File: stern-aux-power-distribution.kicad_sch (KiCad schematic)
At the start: 10 parts, among them J1 Conn_01x04, J2 Conn_01x02_Pin, J3 Conn_01x02_Pin, J4 Conn_01x02_Pin, J5 Conn_01x02_Pin

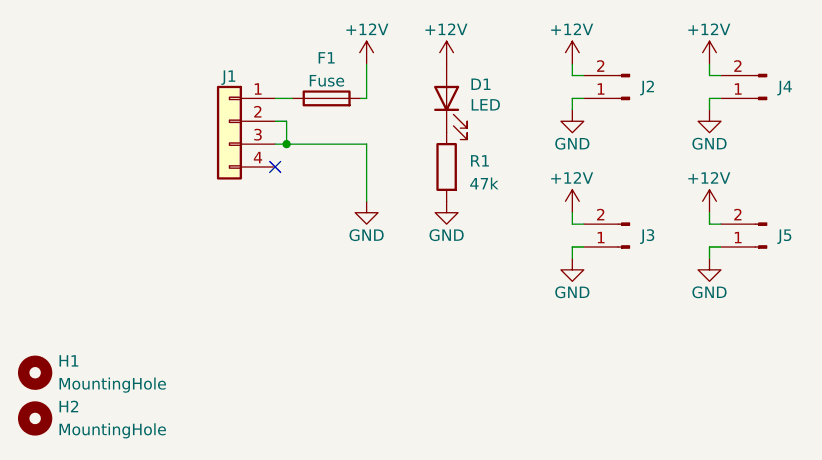
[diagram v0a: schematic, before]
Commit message: More silkscreen info
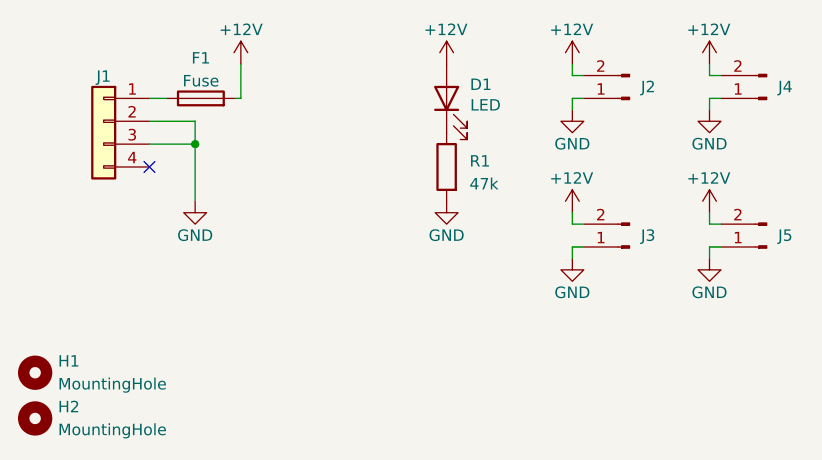
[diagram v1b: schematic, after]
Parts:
- H1, H2: footprint MountingHole:MountingHole_4mm -> MountingHole:MountingHole_4.3mm_M4
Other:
- moved on the sheet: F1, J1
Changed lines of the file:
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@@
 	(paper "A4")
 	(junction
-		(at 92.71 43.18)
+		(at 82.55 43.18)
 		(diameter 0)
 		(color 0 0 0 0)
 	)
 	(no_connect
-		(at 91.44 45.72)
+		(at 77.47 45.72)
 	)
 	(wire
@@
 	(wire
 		(pts
-			(xy 92.71 43.18) (xy 101.6 43.18)
+			(xy 86.995 38.1) (xy 87.63 38.1)
 		)
 		(stroke
@@
 	(wire
 		(pts
-			(xy 101.6 49.53) (xy 101.6 43.18)
+			(xy 82.55 49.53) (xy 82.55 43.18)
 		)
 		(stroke
@@
 	(wire
 		(pts
-			(xy 101.6 34.29) (xy 101.6 38.1)
-		)
-		(stroke
-			(width 0)
-			(type default)
-		)
-	)
-	(wire
-		(pts
-			(xy 91.44 40.64) (xy 92.71 40.64)
+			(xy 87.63 34.29) (xy 87.63 38.1)
+		)
+		(stroke
+			(width 0)
+			(type default)
+		)
+	)
+	(wire
+		(pts
+			(xy 77.47 40.64) (xy 82.55 40.64)
 		)
 		(stroke
@@
 	(wire
 		(pts
-			(xy 101.6 38.1) (xy 100.965 38.1)
-		)
-		(stroke
-			(width 0)
-			(type default)
-		)
-	)
-	(wire
-		(pts
-			(xy 91.44 38.1) (xy 93.345 38.1)
-		)
-		(stroke
-			(width 0)
-			(type default)
-		)
-	)
-	(wire
-		(pts
-			(xy 92.71 43.18) (xy 91.44 43.18)
+			(xy 77.47 38.1) (xy 79.375 38.1)
+		)
+		(stroke
+			(width 0)
+			(type default)
+		)
+	)
+	(wire
+		(pts
+			(xy 77.47 43.18) (xy 82.55 43.18)
 		)
 		(stroke
@@
 	(wire
 		(pts
-			(xy 92.71 40.64) (xy 92.71 43.18)
+			(xy 82.55 40.64) (xy 82.55 43.18)
 		)
 		(stroke
@@
 			)
 		)
-		(property "Footprint" "MountingHole:MountingHole_4mm"
+		(property "Footprint" "MountingHole:MountingHole_4.3mm_M4"
 			(at 64.77 73.66 0)
 			(effects
@@
 	(symbol
 		(lib_id "Device:Fuse")
-		(at 97.155 38.1 90)
+		(at 83.185 38.1 90)
 		(unit 1)
 		(exclude_from_sim no)
@@
 		(fields_autoplaced yes)
 		(property "Reference" "F1"
-			(at 97.155 33.6382 90)
+			(at 83.185 33.6382 90)
 			(effects
 				(font
@@
 		)
 		(property "Value" "Fuse"
-			(at 97.155 36.1751 90)
+			(at 83.185 36.1751 90)
 			(effects
 				(font
@@
 		)
 		(property "Footprint" "Custom_parts:Fuse holder Keystone 3557-2"
-			(at 97.155 39.878 90)
+			(at 83.185 39.878 90)
 			(effects
 				(font
@@
 		)
 		(property "Datasheet" "~"
-			(at 97.155 38.1 0)
+			(at 83.185 38.1 0)
 			(effects
 				(font
@@
 		)
 		(property "Description" ""
-			(at 97.155 38.1 0)
+			(at 83.185 38.1 0)
 			(effects
 				(font
@@
 	(symbol
 		(lib_id "power:+12V")
-		(at 101.6 34.29 0)
+		(at 87.63 34.29 0)
 		(unit 1)
 		(exclude_from_sim no)
@@
 		(on_board yes)
 		(dnp no)
-		(property "Reference" "#PWR01"
-			(at 101.6 38.1 0)
+		(property "Reference" "#PWR02"
+			(at 87.63 38.1 0)
 			(effects
 				(font
@@
 		)
 		(property "Value" "+12V"
-			(at 101.6 30.48 0)
+			(at 87.63 30.48 0)
 			(effects
 				(font
@@
 		)
 		(property "Footprint" ""
-			(at 101.6 34.29 0)
+			(at 87.63 34.29 0)
 			(effects
 				(font
@@
 		)
 		(property "Datasheet" ""
-			(at 101.6 34.29 0)
+			(at 87.63 34.29 0)
 			(effects
 				(font
@@
 		)
 		(property "Description" ""
-			(at 101.6 34.29 0)
+			(at 87.63 34.29 0)
 			(effects
 				(font
@@
 			(project ""
 				(path "/4265d214-fcee-41c6-a88d-6c6bd3f38fd2"
-					(reference "#PWR01")
+					(reference "#PWR02")
 					(unit 1)
 				)
@@
 	(symbol
 		(lib_id "Connector_Generic:Conn_01x04")
-		(at 86.36 40.64 0)
+		(at 72.39 40.64 0)
 		(mirror y)
 		(unit 1)
@@
 		(fields_autoplaced yes)
 		(property "Reference" "J1"
-			(at 86.36 35.6672 0)
+			(at 72.39 35.6672 0)
 			(effects
 				(font
@@
 		)
 		(property "Value" "Conn_01x04"
-			(at 86.36 35.6671 0)
+			(at 72.39 35.6671 0)
 			(effects
 				(font
@@
 		)
 		(property "Footprint" "Connector_TE-Connectivity:TE_MATE-N-LOK_350211-1_1x04_P5.08mm_Vertical"
-			(at 86.36 40.64 0)
+			(at 72.39 40.64 0)
 			(effects
 				(font
@@
 		)
 		(property "Datasheet" "~"
-			(at 86.36 40.64 0)
+			(at 72.39 40.64 0)
 			(effects
 				(font
@@
 		)
 		(property "Description" ""
-			(at 86.36 40.64 0)
+			(at 72.39 40.64 0)
 			(effects
 				(font
@@
 			)
 		)
-		(property "Footprint" "MountingHole:MountingHole_4mm"
+		(property "Footprint" "MountingHole:MountingHole_4.3mm_M4"
 			(at 64.77 68.58 0)
 			(effects
@@
 	(symbol
 		(lib_id "power:GND")
-		(at 101.6 49.53 0)
+		(at 82.55 49.53 0)
 		(unit 1)
 		(exclude_from_sim no)
@@
 		(on_board yes)
 		(dnp no)
-		(property "Reference" "#PWR02"
-			(at 101.6 55.88 0)
+		(property "Reference" "#PWR01"
+			(at 82.55 55.88 0)
 			(effects
 				(font
@@
 		)
 		(property "Value" "GND"
-			(at 101.6 53.34 0)
+			(at 82.55 53.34 0)
 			(effects
 				(font
@@
 		)
 		(property "Footprint" ""
-			(at 101.6 49.53 0)
+			(at 82.55 49.53 0)
 			(effects
 				(font
@@
 		)
 		(property "Datasheet" ""
-			(at 101.6 49.53 0)
+			(at 82.55 49.53 0)
 			(effects
 				(font
@@
 		)
 		(property "Description" ""
-			(at 101.6 49.53 0)
+			(at 82.55 49.53 0)
 			(effects
 				(font
@@
 			(project ""
 				(path "/4265d214-fcee-41c6-a88d-6c6bd3f38fd2"
-					(reference "#PWR02")
-					(unit 1)
-				)
+					(reference "#PWR01")
+					(unit 1)
+				)
